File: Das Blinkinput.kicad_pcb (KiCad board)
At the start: 4 copper layers, 25.4 x 50.8 mm, 36 parts, among them P101 CONN_01X02, P102 CONN_01X01, P103 CONN_01X01, P104 CONN_01X01, P105 CONN_01X05, P106 CONN_01X01, P201 CONN_01X01, P301 CONN_01X01, P401 CONN_01X01, P501 CONN_01X01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

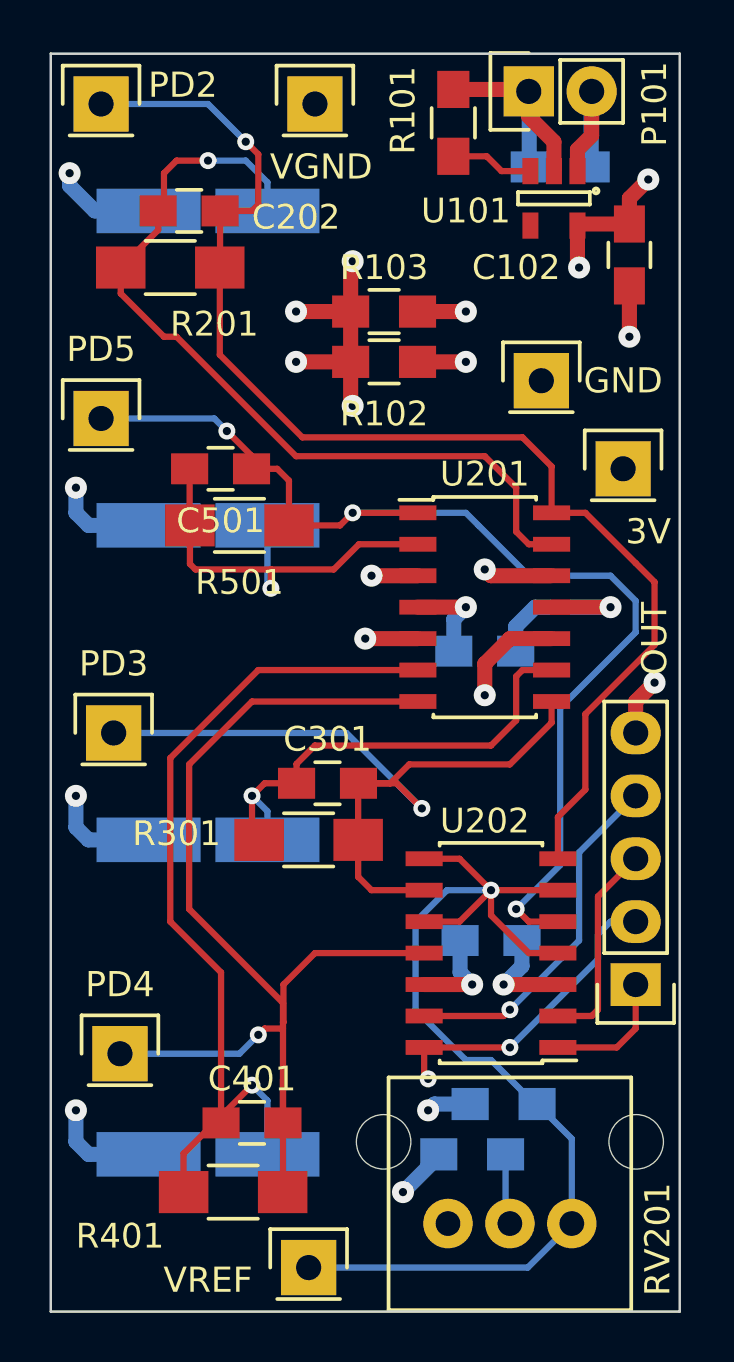
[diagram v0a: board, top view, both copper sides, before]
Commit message: Created DB-CB branch by removing all traces
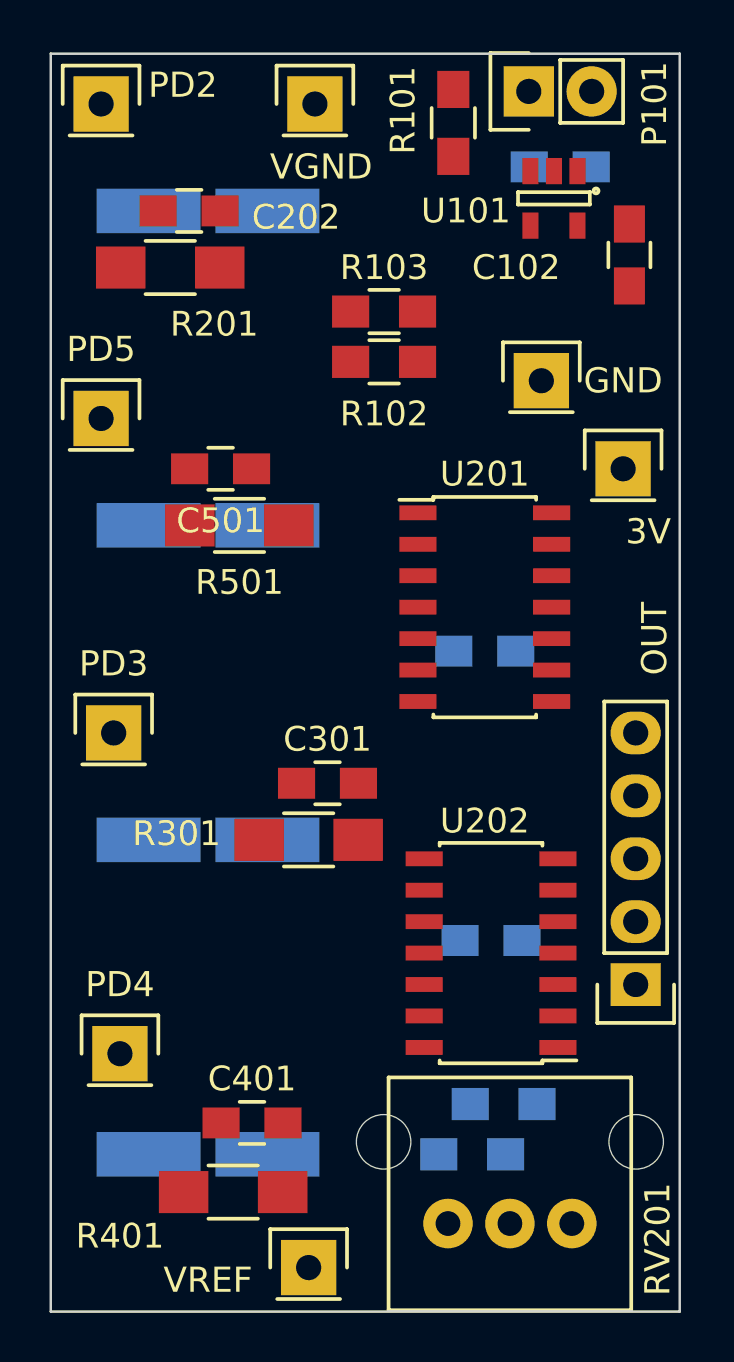
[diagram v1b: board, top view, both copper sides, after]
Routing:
- net Net-(C202-Pad1): track 51.9 -> 0.00 mm, vias 1 -> 0
- net Net-(C401-Pad1): track 45.7 -> 0.00 mm, vias 1 -> 0
- net Net-(C501-Pad1): track 45.4 -> 0.00 mm, vias 3 -> 0
- net /Channel2Photodetect/REF_IN: track 43.9 -> 0.00 mm, vias 1 -> 0
- net VGND: track 38.6 -> 0.00 mm, vias 12 -> 0
- net Net-(C401-Pad2): track 35.7 -> 0.00 mm, vias 1 -> 0
- net Net-(C202-Pad2): track 34.1 -> 0.00 mm, vias 1 -> 0
- net Net-(C301-Pad1): track 33.0 -> 0.00 mm, vias 1 -> 0
- net GND: track 29.5 -> 0.00 mm, vias 6 -> 0
- net Net-(C301-Pad2): track 19.6 -> 0.00 mm, vias 1 -> 0
- net 3V: track 18.2 -> 0.00 mm, vias 6 -> 0
- net Net-(C501-Pad2): track 16.9 -> 0.00 mm, vias 1 -> 0
- net /Channel4Photodetect/PD4: track 14.3 -> 0.00 mm, vias 1 -> 0
- net /Channel2Photodetect/PD3: track 12.6 -> 0.00 mm, vias 2 -> 0
- net /Channel3Photodetect/PD5: track 8.45 -> 0.00 mm
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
